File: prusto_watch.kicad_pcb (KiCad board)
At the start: 2 copper layers, 78.7 x 74.9 mm, 69 parts, among them J1 USB_microB_2040002-1, J2 Conn_02x05_Odd_Even, J3 Vibration Motor, J4 Conn_01x06, J5 Conn_01x08, J6 Conn_01x06, J8 Conn_01x02, J9 Conn_01x04, Q3 RUM002N02T2L, SW1 SW_Push, SW2 SW_Push, U1 STM32F303RCT6-48, U2 TPS2113ADRBR, U3 TSP70933DBVR, U4 MCP73831T-2ACI, U5 TPS60241DGKR, U6 LSM6DSL, U7 RT9818A-18GV, U8 WM1389CT-ND, Y1 ECS.327, Y2 FA-238

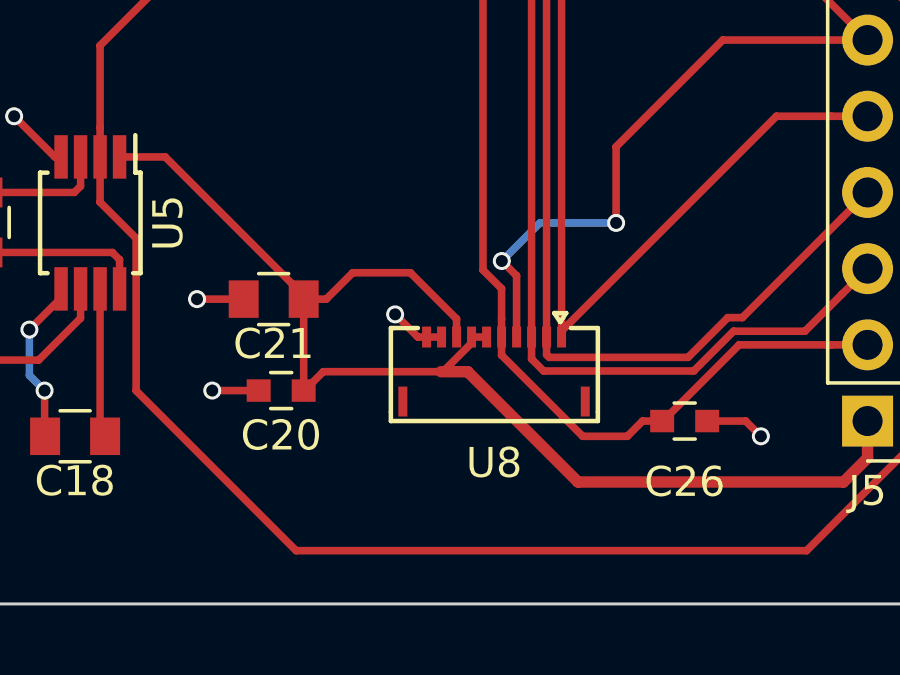
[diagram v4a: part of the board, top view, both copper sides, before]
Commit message: Fix footprint for FPC connector
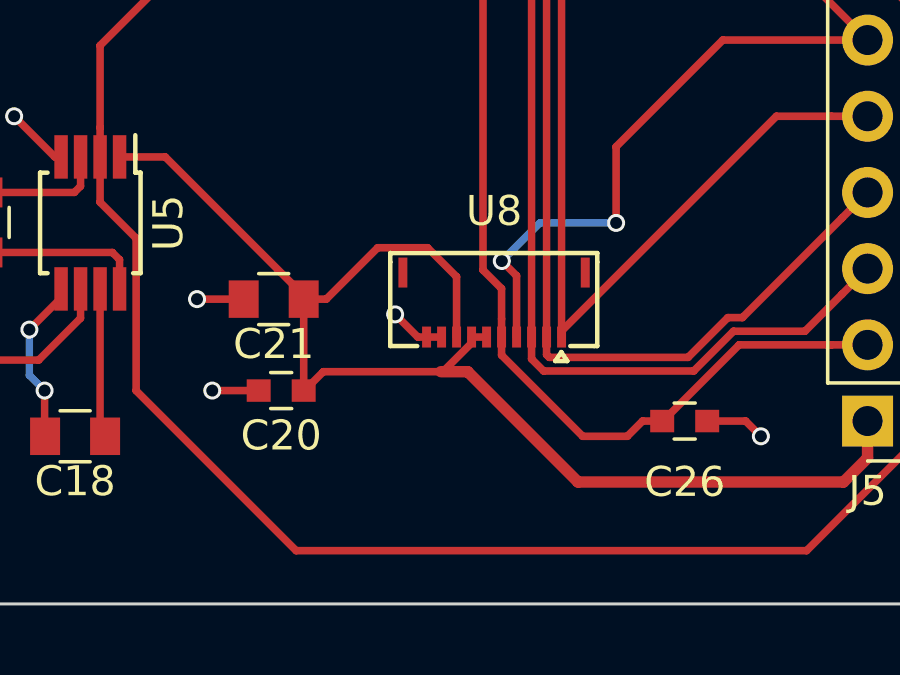
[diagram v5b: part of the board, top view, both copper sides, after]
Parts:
- moved U8 5.60 mm to (98.8, 89.9), turned to 180 degrees
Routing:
- net +5V: track 42.1 -> 43.6 mm
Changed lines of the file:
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@@
   )
   (setup
-    (last_trace_width 0.381)
+    (last_trace_width 0.254)
     (user_trace_width 0.381)
     (user_trace_width 0.508)
@@
       (solder_mask_margin 0.1))
   )
-  (module prusto_watch:Molex_FPC_5034801000 (layer F.Cu)
-    (at 98.802 95.504)
-    (fp_text reference U8 (at 0 1.4) (layer F.SilkS)
-      (effects (font (size 1 1) (thickness 0.15)))
-    )
-    (fp_text value WM1389CT-ND (at 0 -5.1) (layer F.Fab)
-      (effects (font (size 1 1) (thickness 0.15)))
-    )
-    (fp_line (start 3.46 0) (end 3.46 -0.3) (layer F.SilkS) (width 0.15))
-    (fp_line (start -3.44 0) (end 3.46 0) (layer F.SilkS) (width 0.15))
-    (fp_line (start -3.44 -0.3) (end -3.44 0) (layer F.SilkS) (width 0.15))
-    (fp_line (start 2.405 -3.6) (end 2.005 -3.6) (layer F.SilkS) (width 0.15))
-    (fp_line (start 2.205 -3.3) (end 2.405 -3.6) (layer F.SilkS) (width 0.15))
-    (fp_line (start 2.005 -3.6) (end 2.205 -3.3) (layer F.SilkS) (width 0.15))
-    (fp_line (start 3.46 -0.3) (end 3.46 -3.1) (layer F.SilkS) (width 0.15))
-    (fp_line (start 2.56 -3.1) (end 3.46 -3.1) (layer F.SilkS) (width 0.15))
-    (fp_line (start -3.44 -3.1) (end -3.44 -0.3) (layer F.SilkS) (width 0.15))
-    (fp_line (start -3.34 -3.1) (end -3.44 -3.1) (layer F.SilkS) (width 0.15))
-    (fp_line (start -2.54 -3.1) (end -3.34 -3.1) (layer F.SilkS) (width 0.15))
-    (pad "" smd rect (at 3.04 -0.65) (size 0.3 1) (layers F.Cu F.Paste F.Mask))
-    (pad "" smd rect (at -3.04 -0.65) (size 0.3 1) (layers F.Cu F.Paste F.Mask))
-    (pad 10 smd rect (at -2.25 -2.8) (size 0.3 0.7) (layers F.Cu F.Paste F.Mask)
-      (net 2 GND))
-    (pad 9 smd rect (at -1.75 -2.8) (size 0.3 0.7) (layers F.Cu F.Paste F.Mask)
-      (net 2 GND))
-    (pad 8 smd rect (at -1.25 -2.8) (size 0.3 0.7) (layers F.Cu F.Paste F.Mask)
-      (net 15 +5V))
-    (pad 7 smd rect (at -0.75 -2.8) (size 0.3 0.7) (layers F.Cu F.Paste F.Mask)
-      (net 15 +5V))
-    (pad 6 smd rect (at -0.25 -2.8) (size 0.3 0.7) (layers F.Cu F.Paste F.Mask)
-      (net 15 +5V))
-    (pad 5 smd rect (at 0.25 -2.8) (size 0.3 0.7) (layers F.Cu F.Paste F.Mask)
-      (net 17 /DISP_EN))
-    (pad 4 smd rect (at 0.75 -2.8) (size 0.3 0.7) (layers F.Cu F.Paste F.Mask)
-      (net 51 /EXTCOMIN))
-    (pad 3 smd rect (at 1.25 -2.8) (size 0.3 0.7) (layers F.Cu F.Paste F.Mask)
-      (net 50 /DISP_SCS))
-    (pad 2 smd rect (at 1.75 -2.8) (size 0.3 0.7) (layers F.Cu F.Paste F.Mask)
-      (net 47 /DISP_SDI))
-    (pad 1 smd rect (at 2.25 -2.8) (size 0.3 0.7) (layers F.Cu F.Paste F.Mask)
-      (net 45 /DISP_SCLK))
-  )
   (module Pin_Headers:Pin_Header_Straight_1x02_Pitch2.54mm (layer F.Cu)
     (at 84.328 68.58)
@@
     )
   )
+  (module prusto_watch:Molex_FPC_5034801000 (layer F.Cu)
+    (at 98.802 89.904 180)
+    (fp_text reference U8 (at 0 1.4 180) (layer F.SilkS)
+      (effects (font (size 1 1) (thickness 0.15)))
+    )
+    (fp_text value WM1389CT-ND (at 0 -5.1 180) (layer F.Fab)
+      (effects (font (size 1 1) (thickness 0.15)))
+    )
+    (fp_line (start 3.46 0) (end 3.46 -0.3) (layer F.SilkS) (width 0.15))
+    (fp_line (start -3.44 0) (end 3.46 0) (layer F.SilkS) (width 0.15))
+    (fp_line (start -3.44 -0.3) (end -3.44 0) (layer F.SilkS) (width 0.15))
+    (fp_line (start -2.04 -3.6) (end -2.44 -3.6) (layer F.SilkS) (width 0.15))
+    (fp_line (start -2.24 -3.3) (end -2.04 -3.6) (layer F.SilkS) (width 0.15))
+    (fp_line (start -2.44 -3.6) (end -2.24 -3.3) (layer F.SilkS) (width 0.15))
+    (fp_line (start 3.46 -0.3) (end 3.46 -3.1) (layer F.SilkS) (width 0.15))
+    (fp_line (start 2.56 -3.1) (end 3.46 -3.1) (layer F.SilkS) (width 0.15))
+    (fp_line (start -3.44 -3.1) (end -3.44 -0.3) (layer F.SilkS) (width 0.15))
+    (fp_line (start -3.34 -3.1) (end -3.44 -3.1) (layer F.SilkS) (width 0.15))
+    (fp_line (start -2.54 -3.1) (end -3.34 -3.1) (layer F.SilkS) (width 0.15))
+    (pad "" smd rect (at 3.04 -0.65 180) (size 0.3 1) (layers F.Cu F.Paste F.Mask))
+    (pad "" smd rect (at -3.04 -0.65 180) (size 0.3 1) (layers F.Cu F.Paste F.Mask))
+    (pad 1 smd rect (at -2.25 -2.8 180) (size 0.3 0.7) (layers F.Cu F.Paste F.Mask)
+      (net 45 /DISP_SCLK))
+    (pad 2 smd rect (at -1.75 -2.8 180) (size 0.3 0.7) (layers F.Cu F.Paste F.Mask)
+      (net 47 /DISP_SDI))
+    (pad 3 smd rect (at -1.25 -2.8 180) (size 0.3 0.7) (layers F.Cu F.Paste F.Mask)
+      (net 50 /DISP_SCS))
+    (pad 4 smd rect (at -0.75 -2.8 180) (size 0.3 0.7) (layers F.Cu F.Paste F.Mask)
+      (net 51 /EXTCOMIN))
+    (pad 5 smd rect (at -0.25 -2.8 180) (size 0.3 0.7) (layers F.Cu F.Paste F.Mask)
+      (net 17 /DISP_EN))
+    (pad 6 smd rect (at 0.25 -2.8 180) (size 0.3 0.7) (layers F.Cu F.Paste F.Mask)
+      (net 15 +5V))
+    (pad 7 smd rect (at 0.75 -2.8 180) (size 0.3 0.7) (layers F.Cu F.Paste F.Mask)
+      (net 15 +5V))
+    (pad 8 smd rect (at 1.25 -2.8 180) (size 0.3 0.7) (layers F.Cu F.Paste F.Mask)
+      (net 15 +5V))
+    (pad 9 smd rect (at 1.75 -2.8 180) (size 0.3 0.7) (layers F.Cu F.Paste F.Mask)
+      (net 2 GND))
+    (pad 10 smd rect (at 2.25 -2.8 180) (size 0.3 0.7) (layers F.Cu F.Paste F.Mask)
+      (net 2 GND))
+  )
   (gr_text "PrustoWatch\nv0.2\nBW" (at 149.86 31.75) (layer F.SilkS)
     (effects (font (size 1.5 1.5) (thickness 0.3)) (justify right))
@@
   (segment (start 114.046 34.29) (end 113.03 34.29) (width 0.381) (layer F.Cu) (net 1))
   (segment (start 118.28 35.24) (end 114.996 35.24) (width 0.381) (layer F.Cu) (net 1))
+  (segment (start 96.26 92.704) (end 95.504 91.948) (width 0.254) (layer F.Cu) (net 2))
+  (segment (start 96.552 92.704) (end 96.26 92.704) (width 0.254) (layer F.Cu) (net 2))
+  (via (at 95.504 91.948) (size 0.6) (drill 0.4) (layers F.Cu B.Cu) (net 2))
+  (segment (start 97.052 92.704) (end 96.552 92.704) (width 0.254) (layer F.Cu) (net 2))
   (segment (start 81.20851 59.69) (end 80.95451 59.944) (width 0.254) (layer F.Cu) (net 2))
   (via (at 80.95451 59.944) (size 0.6) (drill 0.4) (layers F.Cu B.Cu) (net 2))
@@
   (segment (start 79.264 91.964) (end 78.74 91.44) (width 0.254) (layer F.Cu) (net 2))
   (via (at 78.74 91.44) (size 0.6) (drill 0.4) (layers F.Cu B.Cu) (net 2))
-  (segment (start 96.26 92.704) (end 95.504 91.948) (width 0.254) (layer F.Cu) (net 2))
-  (segment (start 96.552 92.704) (end 96.26 92.704) (width 0.254) (layer F.Cu) (net 2))
-  (via (at 95.504 91.948) (size 0.6) (drill 0.4) (layers F.Cu B.Cu) (net 2))
-  (segment (start 97.052 92.704) (end 96.552 92.704) (width 0.254) (layer F.Cu) (net 2))
   (segment (start 90.456 91.44) (end 88.9 91.44) (width 0.254) (layer F.Cu) (net 2))
   (via (at 88.9 91.44) (size 0.6) (drill 0.4) (layers F.Cu B.Cu) (net 2))
@@
   (segment (start 84.81 87.884) (end 85.019 87.675) (width 0.25) (layer F.Cu) (net 14))
   (segment (start 85.019 87.675) (end 85.019 86.7) (width 0.25) (layer F.Cu) (net 14))
-  (segment (start 97.552 92.1) (end 97.552 92.704) (width 0.254) (layer F.Cu) (net 15))
-  (segment (start 96.013 90.561) (end 97.552 92.1) (width 0.254) (layer F.Cu) (net 15))
-  (segment (start 94.089 90.561) (end 96.013 90.561) (width 0.254) (layer F.Cu) (net 15))
-  (segment (start 93.21 91.44) (end 94.089 90.561) (width 0.254) (layer F.Cu) (net 15))
-  (segment (start 92.456 91.44) (end 93.21 91.44) (width 0.254) (layer F.Cu) (net 15))
+  (segment (start 97.552 92.704) (end 97.552 90.694) (width 0.254) (layer F.Cu) (net 15))
+  (segment (start 97.552 90.694) (end 96.584999 89.726999) (width 0.254) (layer F.Cu) (net 15))
+  (segment (start 96.584999 89.726999) (end 94.923001 89.726999) (width 0.254) (layer F.Cu) (net 15))
+  (segment (start 94.923001 89.726999) (end 93.21 91.44) (width 0.254) (layer F.Cu) (net 15))
+  (segment (start 93.21 91.44) (end 92.456 91.44) (width 0.254) (layer F.Cu) (net 15))
   (segment (start 98.052 92.704) (end 98.552 92.704) (width 0.254) (layer F.Cu) (net 15))
   (segment (start 97.097 93.859) (end 97.028 93.859) (width 0.254) (layer F.Cu) (net 15))

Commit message: Modify schematic
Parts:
- removed C22, C23: 100nF, Capacitors_SMD:C_0603
- removed D5, D6: LED, LEDs:LED_0805_HandSoldering
- removed J8: Conn_01x02, Pin_Headers:Pin_Header_Straight_1x02_Pitch2.54mm
- removed J9: Conn_01x04, Pin_Headers:Pin_Header_Straight_1x04_Pitch2.54mm
- removed R10: 10K, Resistors_SMD:R_0603
- removed R12: DNP-0, Resistors_SMD:R_0603
- removed R7: 470, Resistors_SMD:R_0603
- removed R8: 1K, Resistors_SMD:R_0603
- removed SW1: SW_Push, prusto_watch:PTS820_J15M_SMTR_LFS
- removed U4: MCP73831T-2ACI, TO_SOT_Packages_SMD:SOT-23-5
- removed U6: LSM6DSL, Housings_LGA:Bosch_LGA-14_3x2.5mm_Pitch0.5mm
- C12: value 2.2uF -> 10uF
- C14: value 4.7uF -> 100nF
- C8: value 4.7uF -> 2.2uF
- J4: footprint Pin_Headers:Pin_Header_Straight_1x06_Pitch2.54mm -> Pin_Headers:Pin_Header_Straight_2x03_Pitch1.27mm
- J5: footprint Pin_Headers:Pin_Header_Straight_1x08_Pitch2.54mm -> Pin_Headers:Pin_Header_Straight_2x04_Pitch1.27mm
- J6: value Conn_01x06 -> Conn_02x03_Odd_Even; footprint Pin_Headers:Pin_Header_Straight_1x06_Pitch2.54mm -> Pin_Headers:Pin_Header_Straight_2x03_Pitch1.27mm
- R2: value 1K -> 715
- R4: value 100K -> 1K
- R5: value 402 -> 440K
- R6: value 200K -> 160K
- U2: value TPS2113ADRBR -> LTC4063; footprint prusto_watch:SON-8 -> Housings_DFN_QFN:DFN-10-1EP_3x3mm_Pitch0.5mm
- U3: value TSP70933DBVR -> LIS3DETR; footprint TO_SOT_Packages_SMD:SOT-23-5 -> prusto_watch:16-LGA_(3x3)
- moved U3 42.8 mm to (98.6, 17.5)
- moved U2 12.8 mm to (145.2, 45.4)
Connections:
- BT1 pad 1: /VBATT -> Net-(BT1-Pad1)
- C12 pad 1: Net-(C12-Pad1) -> +3V3
- C14 pad 1: /VBATT -> +3V3
- C5 pad 1: /VBATT -> Net-(BT1-Pad1)
- C6 pad 1: /VUSB -> Net-(C6-Pad1)
- C7 pad 1: Net-(C7-Pad1) -> Net-(C6-Pad1)
- C8 pad 1: /VUSB -> +3V3
- D1 pad 2: /VUSB -> +3V3
- FP1 pad 1: Net-(FP1-Pad1) -> (no net)
- FP1 pad 11: Net-(FP1-Pad11) -> (no net)
- FP1 pad 15: Net-(FP1-Pad15) -> (no net)
- FP1 pad 3: Net-(FP1-Pad3) -> (no net)
- FP1 pad 4: Net-(FP1-Pad4) -> (no net)
- FP1 pad 5: Net-(FP1-Pad5) -> (no net)
- FP1 pad 6: Net-(FP1-Pad6) -> (no net)
- FP1 pad 9: Net-(FP1-Pad9) -> (no net)
- J1 pad 1: /VUSB -> Net-(C6-Pad1)
- J1 pad 2: /D_N -> (no net)
- J1 pad 3: /D_P -> (no net)
- J1 pad 4: Net-(J1-Pad4) -> (no net)
- J2 pad 7: Net-(J2-Pad7) -> (no net)
- J2 pad 9: Net-(J2-Pad9) -> (no net)
- J6 pad 2: Net-(J6-Pad2) -> /ACC_SCK
- J6 pad 3: /TSC_G5_IO2 -> /ACC_CS
- J6 pad 4: /TSC_G5_IO3 -> /ACC_SDI
- J6 pad 5: /TSC_G5_IO4 -> GND
- J6 pad 6: GND -> /ACC_SDO
- R2 pad 1: Net-(D5-Pad1) -> Net-(R2-Pad1)
- R2 pad 2: /LED_2 -> GND
- R3 pad 1: Net-(R3-Pad1) -> +3V3
- R4 pad 1: Net-(R4-Pad1) -> Net-(D1-Pad1)
- R4 pad 2: GND -> /CHRG_STAT
- R5 pad 1: Net-(R5-Pad1) -> +3V3
- R5 pad 2: GND -> Net-(R5-Pad2)
- R6 pad 1: /VUSB -> Net-(R5-Pad2)
- R6 pad 2: Net-(R4-Pad1) -> GND
- U1 pad 14: Net-(U1-Pad14) -> (no net)
- U1 pad 16: Net-(U1-Pad16) -> (no net)
- U1 pad 18: /LED_3 -> (no net)
- U1 pad 25: Net-(U1-Pad25) -> (no net)
- U1 pad 26: /IMU_SCL -> (no net)
- U1 pad 27: /IMU_SDO -> (no net)
- U1 pad 28: /IMU_SDI -> (no net)
- U1 pad 29: /IMU_CS -> (no net)
- U1 pad 30: /IMU_INT_1 -> (no net)
- U1 pad 31: /IMU_INT_2 -> (no net)
- U1 pad 32: /D_N -> (no net)
- U1 pad 33: /D_P -> (no net)
- U1 pad 40: /TSC_G5_IO2 -> (no net)
- U1 pad 41: Net-(U1-Pad41) -> (no net)
- U1 pad 42: /TSC_G5_IO3 -> (no net)
- U1 pad 43: /TSC_G5_IO4 -> (no net)
- U1 pad 44: Net-(R3-Pad1) -> +3V3
- U1 pad 45: /LED_2 -> (no net)
- U2 pad 1: Net-(U2-Pad1) -> Net-(BT1-Pad1)
- U2 pad 2: GND -> +3V3
- U2 pad 3: Net-(R4-Pad1) -> Net-(R5-Pad2)
- U2 pad 4: Net-(R5-Pad1) -> (no net)
- U2 pad 5: GND -> (no net)
- U2 pad 6: /VBATT -> /CHRG_STAT
- U2 pad 7: Net-(C7-Pad1) -> GND
- U2 pad 8: /VUSB -> Net-(R2-Pad1)
- U3 pad 1: Net-(C7-Pad1) -> +3V3
- U3 pad 2: GND -> (no net)
- U3 pad 3: Net-(C7-Pad1) -> (no net)
- U3 pad 4: Net-(U3-Pad4) -> /ACC_SCK
- U3 pad 5: Net-(C12-Pad1) -> GND
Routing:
- net /VUSB: track 68.5 -> 0.00 mm, vias 2 -> 0
- net /D_N: track 53.0 -> 0.00 mm, vias 1 -> 0
- net (no net): track 0.00 -> 49.6 mm, vias 0 -> 8
- net /D_P: track 47.8 -> 0.00 mm
- net +3V3: track 339.8 -> 294.4 mm, vias 8 -> 6
- net /IMU_SDO: track 34.2 -> 0.00 mm, vias 2 -> 0
- net /LED_3: track 33.9 -> 0.00 mm, vias 4 -> 0
- net /VBATT: track 32.0 -> 0.00 mm
- net /IMU_CS: track 31.1 -> 0.00 mm, vias 4 -> 0
- net /LED_2: track 29.8 -> 0.00 mm, vias 2 -> 0
- net /TSC_G5_IO2: track 28.4 -> 0.00 mm, vias 2 -> 0
- net /IMU_SCL: track 27.6 -> 0.00 mm, vias 6 -> 0
- net /TSC_G5_IO3: track 26.3 -> 0.00 mm, vias 2 -> 0
- net /IMU_SDI: track 25.4 -> 0.00 mm, vias 4 -> 0
- net /TSC_G5_IO4: track 24.7 -> 0.00 mm, vias 2 -> 0
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
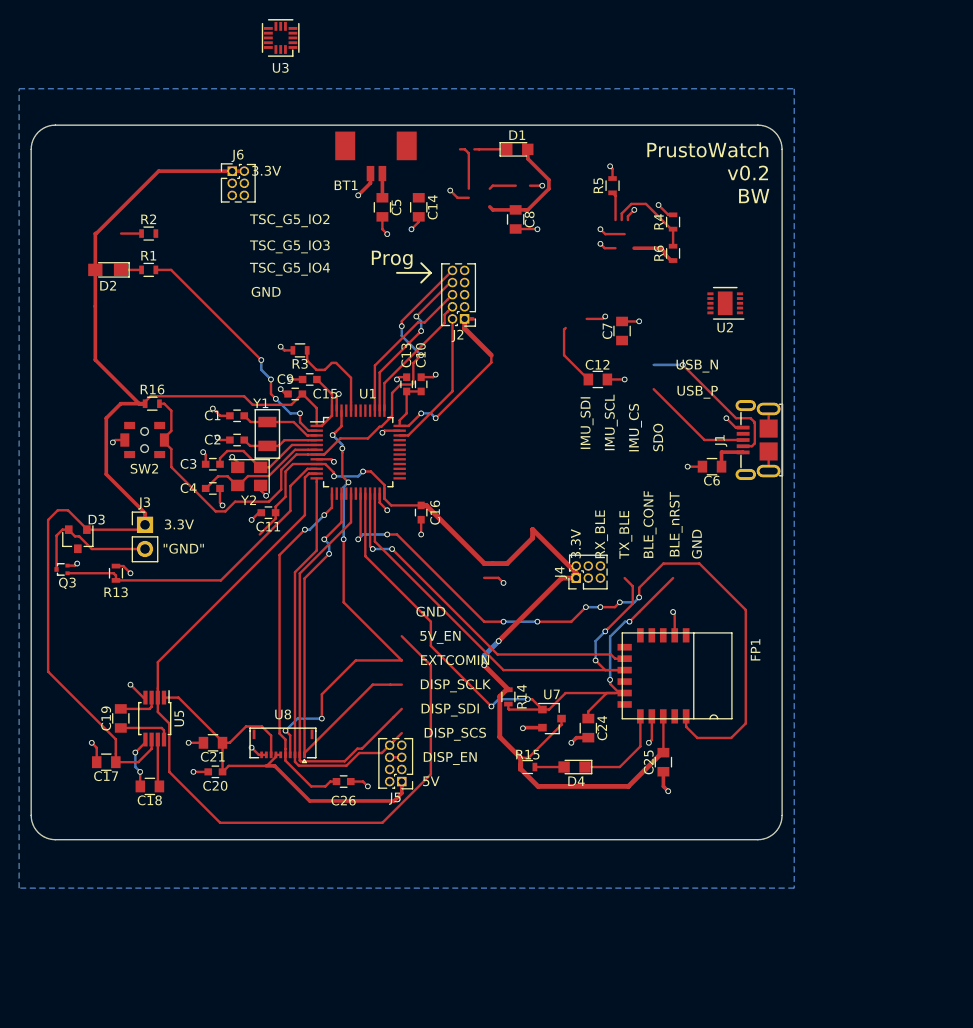
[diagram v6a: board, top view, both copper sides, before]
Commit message: Finish schematic for v3
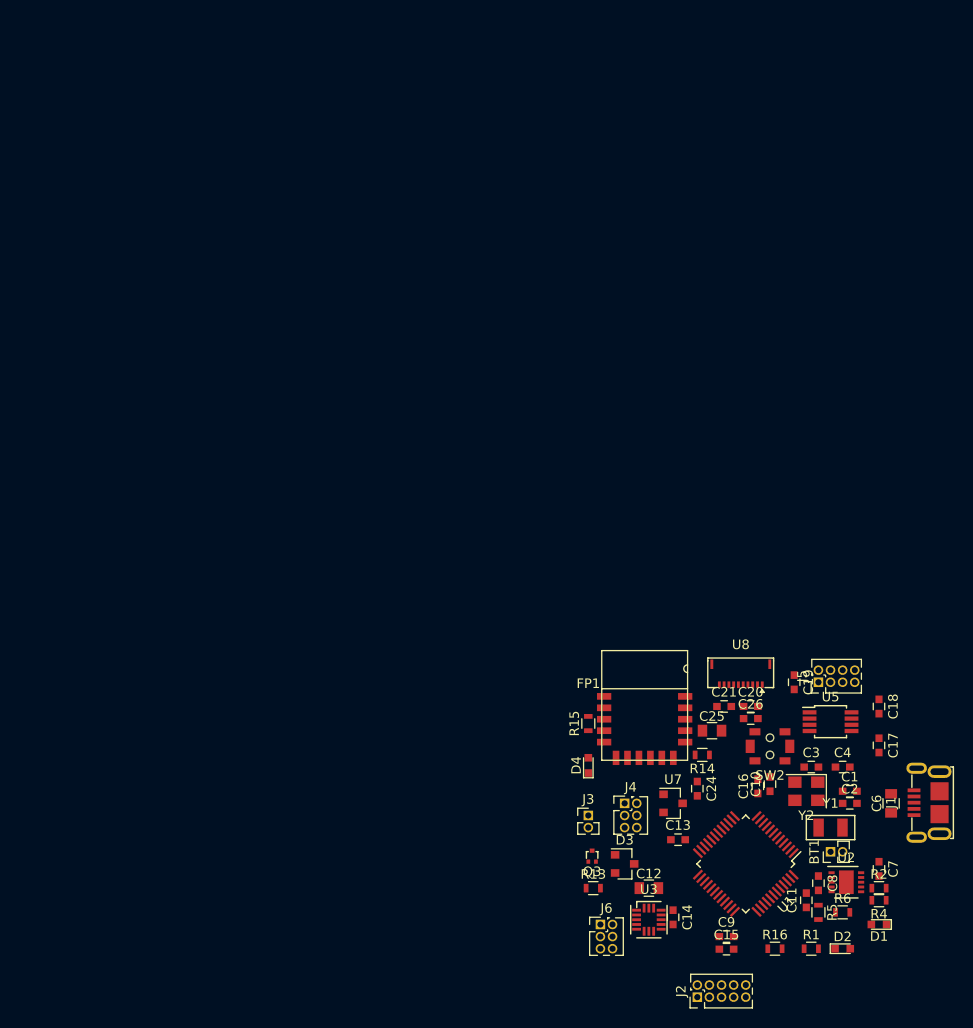
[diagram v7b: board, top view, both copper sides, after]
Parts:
- removed C5: 4.7uF, Capacitors_SMD:C_0805
- removed R3: 10K, Resistors_SMD:R_0603
- BT1: footprint prusto_watch:Molex-0532610271 -> Pin_Headers:Pin_Header_Straight_1x02_Pitch1.27mm
- C14, C17, C18, C19, C21, C24, C7, C8: footprint Capacitors_SMD:C_0805 -> Capacitors_SMD:C_0603
- D1, D4: footprint LEDs:LED_0805 -> LEDs:LED_0603
- D2: footprint LEDs:LED_0805_HandSoldering -> LEDs:LED_0603
- J3: footprint Pin_Headers:Pin_Header_Straight_1x02_Pitch2.54mm -> Pin_Headers:Pin_Header_Straight_1x02_Pitch1.27mm
- R5: value 440K -> 301K
- R6: value 160K -> 100K
- moved D2 104.9 mm to (157.5, 113.0), turned to 0 degrees
- moved R2 102.8 mm to (161.3, 106.7)
- moved U3 100.2 mm to (137.2, 110.0), turned to 0 degrees
- moved R1 99.5 mm to (154.2, 113.0)
- moved D1 89.7 mm to (161.3, 110.5), turned to 180 degrees
- moved J6 87.9 mm to (132.1, 110.5)
- moved R16 86.8 mm to (150.4, 113.0)
- moved BT1 85.2 mm to (156.2, 102.9), turned to 90 degrees
- moved C17 81.0 mm to (161.3, 91.7), turned to 270 degrees
- moved R5 79.2 mm to (154.9, 109.2), turned to 270 degrees
- moved C14 79.1 mm to (139.7, 109.7)
- moved C18 76.9 mm to (161.3, 87.6), turned to 270 degrees
- moved C8 76.5 mm to (154.9, 106.2)
- moved C1 75.4 mm to (158.2, 96.5), turned to 0 degrees
- moved J2 75.2 mm to (142.2, 118.1), turned to 90 degrees
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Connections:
- U1 pad 26: (no net) -> /ACC_SCK
- U1 pad 27: (no net) -> /ACC_SDO
- U1 pad 28: (no net) -> /ACC_SDI
- U1 pad 29: (no net) -> /ACC_CS
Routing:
- net +3V3: track 294.4 -> 0.00 mm, vias 6 -> 0
- net /5V_EN: track 86.6 -> 0.00 mm
- net /BLE_CONF: track 75.0 -> 0.00 mm, vias 8 -> 0
- net GND: track 74.3 -> 0.00 mm, vias 39 -> 0
- net /BLE_nRST: track 67.7 -> 0.00 mm, vias 4 -> 0
- net /STM_NRST: track 58.8 -> 0.00 mm, vias 2 -> 0
- net /TX_BLE: track 50.9 -> 0.00 mm, vias 2 -> 0
- net /EXTCOMIN: track 50.7 -> 0.00 mm, vias 6 -> 0
- net (no net): track 49.6 -> 0.00 mm, vias 8 -> 0
- net +5V: track 43.6 -> 0.00 mm
- net /DISP_SCS: track 43.4 -> 0.00 mm
- net /DISP_SDI: track 43.2 -> 0.00 mm
- net /DISP_SCLK: track 42.8 -> 0.00 mm, vias 2 -> 0
- net /DISP_EN: track 37.5 -> 0.00 mm, vias 2 -> 0
- net /RX_BLE: track 37.1 -> 0.00 mm, vias 2 -> 0
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- removed copper zone on B.Cu, net GND
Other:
- board outline removed
- net class Default: trace_width 0.254 -> 0.25
- board text removed: ""GND""
- board text removed: "3.3V"
- board text removed: "5V"
- board text removed: "5V_EN"
- board text removed: "BLE_CONF"
- board text removed: "BLE_nRST"
- board text removed: "DISP_EN"
- board text removed: "DISP_SCLK"
- board text removed: "DISP_SCS"
- board text removed: "DISP_SDI"
- board text removed: "EXTCOMIN"
- board text removed: "GND"
- board text removed: "IMU_CS"
- board text removed: "IMU_SCL"
- board text removed: "IMU_SDI"
- board text removed: "Prog"
- board text removed: "PrustoWatch v0.2 BW"
- board text removed: "RX_BLE"
- board text removed: "SDO"
- board text removed: "TSC_G5_IO2"
- board text removed: "TSC_G5_IO3"
- board text removed: "TSC_G5_IO4"
- board text removed: "TX_BLE"
- board text removed: "USB_N"
- board text removed: "USB_P"
